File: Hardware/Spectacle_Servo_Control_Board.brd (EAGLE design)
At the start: 25.4 x 55.9 mm, 49 parts, among them J1 FTDI_DEVICE, J10 AUDIO-JACK3, J3 USB-MICROB, J4 AUDIO-JACK3, U1 CY8C4146LQI-S422, U2 3.3V/150mA

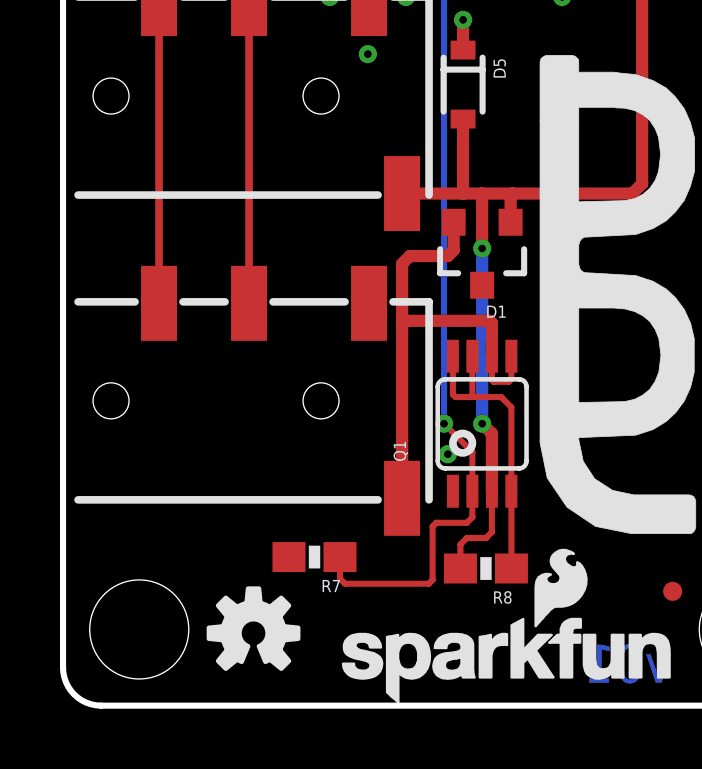
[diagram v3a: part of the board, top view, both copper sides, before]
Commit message: Add servo.h, .project, in/out labels
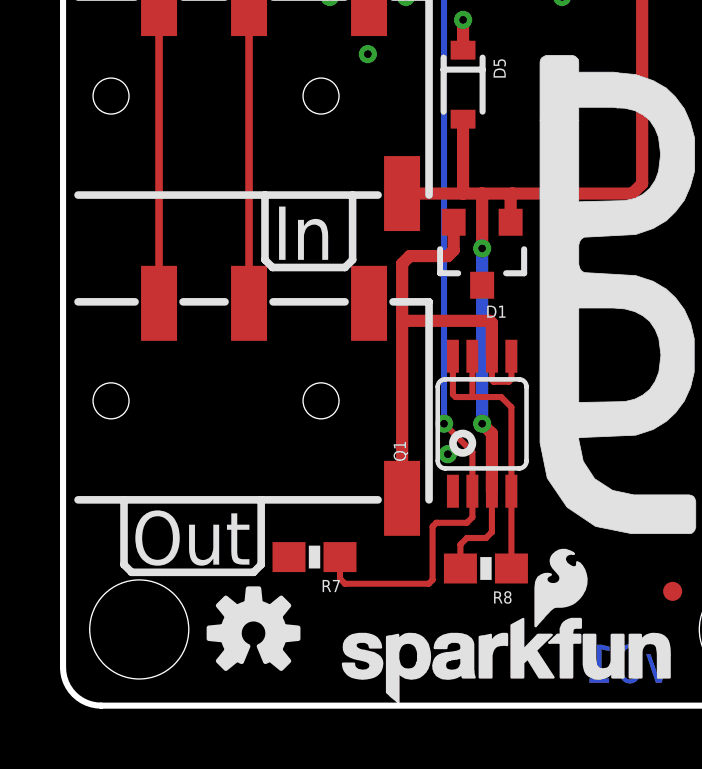
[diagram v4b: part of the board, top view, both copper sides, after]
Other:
- board text added: "In"
- board text added: "Out"
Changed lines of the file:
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@@
 <text x="0.381" y="46.482" size="1.016" layer="21" font="vector" ratio="15">O/W/Y</text>
 <text x="20.574" y="46.482" size="1.016" layer="21" font="vector" ratio="15">O/W/Y</text>
+<text x="6.985" y="14.859" size="1.778" layer="21" font="vector" ratio="15">In</text>
+<text x="2.286" y="4.699" size="1.778" layer="21" font="vector" ratio="15">Out</text>
+<wire x1="2.032" y1="6.858" x2="2.032" y2="4.699" width="0.254" layer="21"/>
+<wire x1="2.032" y1="4.699" x2="2.286" y2="4.445" width="0.254" layer="21"/>
+<wire x1="2.286" y1="4.445" x2="6.35" y2="4.445" width="0.254" layer="21"/>
+<wire x1="6.35" y1="4.445" x2="6.604" y2="4.699" width="0.254" layer="21"/>
+<wire x1="6.604" y1="4.699" x2="6.604" y2="6.858" width="0.254" layer="21"/>
+<wire x1="6.731" y1="17.018" x2="6.731" y2="14.859" width="0.254" layer="21"/>
+<wire x1="6.731" y1="14.859" x2="6.985" y2="14.605" width="0.254" layer="21"/>
+<wire x1="6.985" y1="14.605" x2="9.398" y2="14.605" width="0.254" layer="21"/>
+<wire x1="9.398" y1="14.605" x2="9.652" y2="14.859" width="0.254" layer="21"/>
+<wire x1="9.652" y1="14.859" x2="9.652" y2="17.018" width="0.254" layer="21"/>
 </plain>
 <attributes>
